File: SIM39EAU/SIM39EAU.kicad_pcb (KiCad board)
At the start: 2 copper layers, 30.5 x 25.4 mm, 17 parts, among them IC1 SIM39EA, J1 Conn_01x08, U2 AP7365-W-7

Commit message: LED Update
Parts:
- removed R7: 68K, Resistor_SMD:R_0603_1608Metric
- removed R8: 22K, Resistor_SMD:R_0603_1608Metric
- removed U2: AP7365-W-7, Package_TO_SOT_SMD:SOT-23-5
- added 3.3V: LED, LED_SMD:LED_0603_1608Metric, F.Cu at (53.1, 33.0)
- added LED: SolderJumper_2_Bridged, Jumper:SolderJumper-2_P1.3mm_Bridged_RoundedPad1.0x1.5mm, B.Cu at (56.3, 38.9)
- added R1: 680E, Resistor_SMD:R_0603_1608Metric, F.Cu at (53.1, 36.3)
- added U1: AP2127K-3.3, Package_TO_SOT_SMD:SOT-23-5, F.Cu at (55.8, 35.3)
- C4: value 1uF -> 4.7uF
- moved G*** 0.18 mm to (56.0, 27.3)
- renumbered CR1220 to BT1
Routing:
- net Net-(JP1-Pad2): track 0.00 -> 3.99 mm, vias 0 -> 1
- net Net-(R7-Pad2): track 3.84 -> 0.00 mm
- net Net-(D3-Pad2): track 0.00 -> 1.75 mm
- net 3V3: track 5.04 -> 3.92 mm, vias 3 -> 2

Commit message: Schematic PDF and 3D Renders added
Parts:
- renumbered BT1 to CR1220
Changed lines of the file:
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@@
   )
   (setup
-    (last_trace_width 0.4)
+    (last_trace_width 0.127)
     (user_trace_width 0.127)
     (user_trace_width 0.15)
@@
     (tags "Keystone type 3000 coin cell retainer")
     (attr smd)
-    (fp_text reference BT1 (at 0 4.445 270 unlocked) (layer B.SilkS)
+    (fp_text reference CR1220 (at 0 4.445 270 unlocked) (layer B.SilkS)
       (effects (font (size 1 1) (thickness 0.15)) (justify mirror))
     )

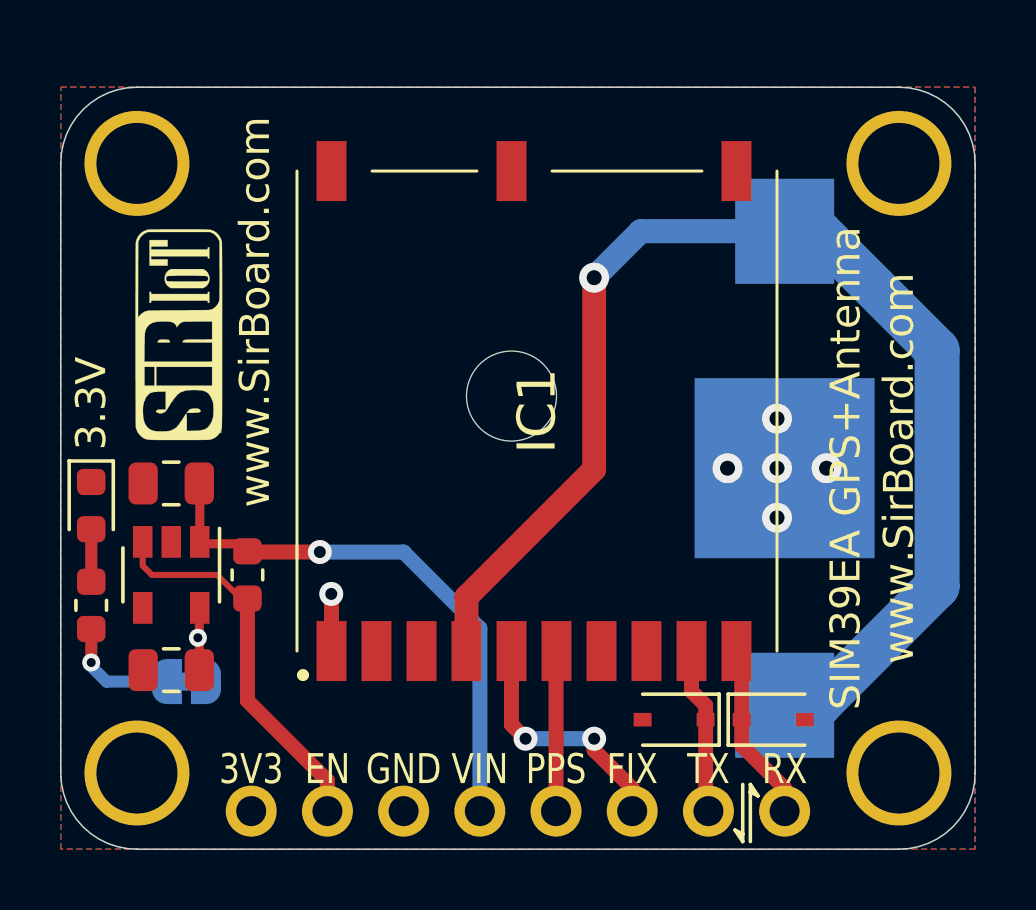
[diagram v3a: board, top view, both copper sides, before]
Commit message: Board Sizes Updated
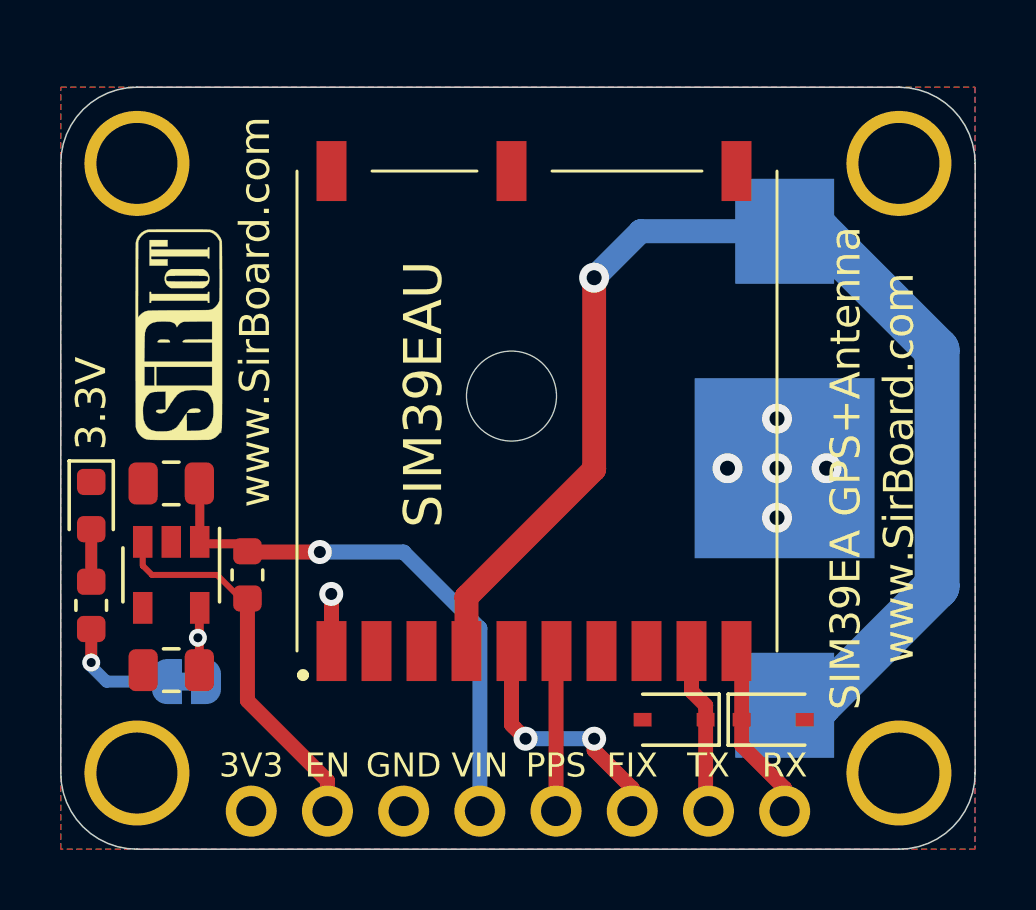
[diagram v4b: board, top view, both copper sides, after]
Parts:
- renumbered IC1 to SIM39EAU
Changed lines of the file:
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@@
   (general
     (thickness 1.6)
-    (drawings 34)
+    (drawings 26)
     (tracks 67)
     (zones 0)
@@
     (38 B.Mask user hide)
     (39 F.Mask user hide)
-    (40 Dwgs.User user hide)
+    (40 Dwgs.User user)
     (41 Cmts.User user hide)
     (42 Eco1.User user hide)
@@
     (descr SIM39EA-2)
     (tags "Integrated Circuit")
-    (fp_text reference IC1 (at 0 0 90) (layer F.SilkS)
+    (fp_text reference SIM39EAU (at 0.5588 -3.7846 90) (layer F.SilkS)
       (effects (font (size 1.27 1.27) (thickness 0.254)))
     )
@@
     )
   )
+  (gr_line (start 54.61 44.45) (end 80.01 44.45) (layer Edge.Cuts) (width 0.05))
   (gr_text www.SirBoard.com (at 58.547 26.543 90) (layer F.SilkS)
     (effects (font (size 1 1) (thickness 0.15)))
@@
     (effects (font (size 1 1) (thickness 0.15)))
   )
-  (gr_line (start 75.057 42.545) (end 75.184 42.545) (layer F.SilkS) (width 0.12))
-  (gr_line (start 75.311 42.672) (end 75.057 42.545) (layer F.SilkS) (width 0.12))
-  (gr_line (start 75.057 42.291) (end 75.311 42.672) (layer F.SilkS) (width 0.12))
-  (gr_line (start 75.057 44.196) (end 75.057 42.291) (layer F.SilkS) (width 0.12))
-  (gr_line (start 74.803 43.942) (end 74.676 43.942) (layer F.SilkS) (width 0.12))
-  (gr_line (start 74.549 43.815) (end 74.803 43.942) (layer F.SilkS) (width 0.12))
-  (gr_line (start 74.803 44.196) (end 74.549 43.815) (layer F.SilkS) (width 0.12))
-  (gr_line (start 74.803 42.291) (end 74.803 44.196) (layer F.SilkS) (width 0.12))
-  (gr_text FIX (at 71.12 41.783) (layer F.SilkS)
-    (effects (font (size 1 0.8) (thickness 0.15)))
+  (gr_text FIX (at 71.12 41.656) (layer F.SilkS)
+    (effects (font (size 0.8 0.8) (thickness 0.12)))
   )
   (dimension 20.32 (width 0.15) (layer Dwgs.User)
@@
     (arrow2b (pts (xy 58.42 46.99) (xy 59.546504 46.403579)))
   )
-  (gr_text VIN (at 66.04 41.783) (layer F.SilkS)
-    (effects (font (size 1 0.8) (thickness 0.15)))
-  )
-  (gr_text GND (at 63.5 41.783) (layer F.SilkS)
-    (effects (font (size 1 0.8) (thickness 0.15)))
-  )
-  (gr_text EN (at 60.96 41.783) (layer F.SilkS)
-    (effects (font (size 1 0.8) (thickness 0.15)))
+  (gr_text VIN (at 66.04 41.656) (layer F.SilkS)
+    (effects (font (size 0.8 0.8) (thickness 0.12)))
+  )
+  (gr_text GND (at 63.5 41.656) (layer F.SilkS)
+    (effects (font (size 0.8 0.8) (thickness 0.12)))
+  )
+  (gr_text EN (at 60.96 41.656) (layer F.SilkS)
+    (effects (font (size 0.8 0.8) (thickness 0.12)))
   )
   (dimension 30.48 (width 0.12) (layer Dwgs.User)
@@
     (arrow2b (pts (xy 86.36 44.45) (xy 85.773579 43.323496)))
   )
-  (gr_text RX (at 76.2 41.783) (layer F.SilkS)
-    (effects (font (size 1 0.8) (thickness 0.15)))
-  )
-  (gr_text PPS (at 68.58 41.783) (layer F.SilkS)
-    (effects (font (size 1 0.8) (thickness 0.15)))
-  )
-  (gr_text TX (at 73.66 41.783) (layer F.SilkS)
-    (effects (font (size 1 0.8) (thickness 0.15)))
-  )
-  (gr_text 3V3 (at 58.42 41.783) (layer F.SilkS)
-    (effects (font (size 1 0.8) (thickness 0.15)))
+  (gr_text RX (at 76.2 41.656) (layer F.SilkS)
+    (effects (font (size 0.8 0.8) (thickness 0.12)))
+  )
+  (gr_text PPS (at 68.58 41.656) (layer F.SilkS)
+    (effects (font (size 0.8 0.8) (thickness 0.12)))
+  )
+  (gr_text TX (at 73.66 41.656) (layer F.SilkS)
+    (effects (font (size 0.8 0.8) (thickness 0.12)))
+  )
+  (gr_text 3V3 (at 58.42 41.656) (layer F.SilkS)
+    (effects (font (size 0.8 0.8) (thickness 0.12)))
   )
   (gr_line (start 52.07 21.59) (end 52.07 41.91) (layer Edge.Cuts) (width 0.05))
@@
   (gr_line (start 82.55 41.91) (end 82.55 21.59) (layer Edge.Cuts) (width 0.05))
   (gr_arc (start 80.01 41.91) (end 80.01 44.45) (angle -90) (layer Edge.Cuts) (width 0.05))
-  (gr_line (start 54.61 44.45) (end 80.01 44.45) (layer Edge.Cuts) (width 0.05))
   (gr_arc (start 54.61 41.91) (end 52.07 41.91) (angle -90) (layer Edge.Cuts) (width 0.05))
   (via (at 75.946 31.75) (size 1) (drill 0.5) (layers F.Cu B.Cu) (net 1))
@@
   (segment (start 53.086 38.354) (end 53.594 38.862) (width 0.4) (layer B.Cu) (net 13))
   (zone (net 1) (net_name GND) (layer F.Cu) (hatch none 0.508)
-    (connect_pads (clearance 0.15))
+    (connect_pads (clearance 0.2))
     (min_thickness 0.15)
     (fill yes (arc_segments 32) (thermal_gap 0.2) (thermal_bridge_width 0.25))

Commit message: Soldermask width adjusted
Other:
- rule solder_mask_min_width: 0.1 -> 0.05
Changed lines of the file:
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@@
     (pad_drill 1)
     (pad_to_mask_clearance 0)
-    (solder_mask_min_width 0.1)
+    (solder_mask_min_width 0.05)
     (aux_axis_origin 0 0)
     (visible_elements 7FFFFFFF)

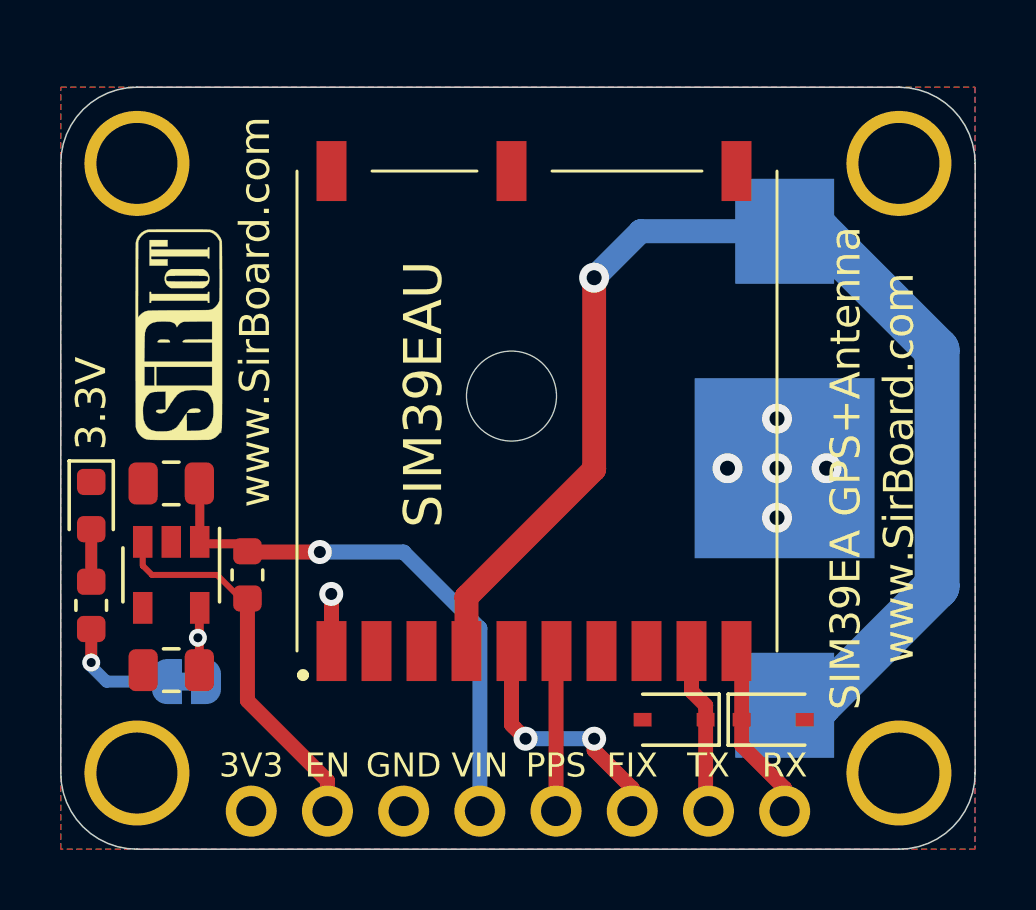
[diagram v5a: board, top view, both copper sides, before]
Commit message: SIM39EA Revision 2
Battery connector changed and silkscreens rearranged
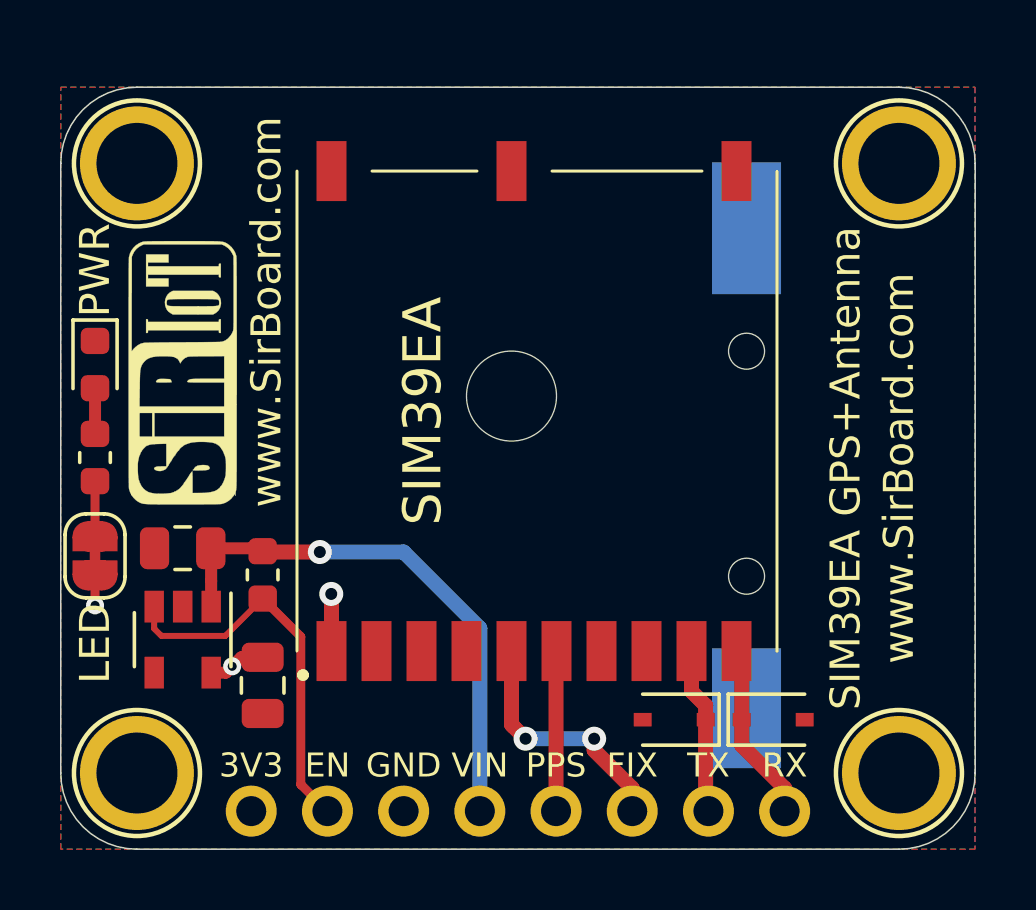
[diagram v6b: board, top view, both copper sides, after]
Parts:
- added G***: LOGO, logo:logo94x134, B.Cu at (62.7, 29.5)
- added REF**: OSHW-Logo2_7.3x6mm_SilkScreen, Symbol:OSHW-Logo2_7.3x6mm_SilkScreen, B.Cu at (56.1, 29.6)
- C3: value 1uF -> 10uF
- C4: value 4.7uF -> 10uF
- CR1220: footprint Battery:BatteryHolder_Keystone_3000_1x12mm -> SirBoardLibrary:S8411-45R_1
- G***: footprint logo:SirIoT98x40 -> logo:SirBoard140x44
- G***: footprint logo:SirIoT70x29 -> logo:SirIoT88x36
- H1, H2, H3, H4: footprint MountingHole:MountingHole_2.7mm_M2.5_ISO14580_Pad -> SirBoardLibrary:MountingHole_M2.5_SirBoard
- LED: footprint Jumper:SolderJumper-2_P1.3mm_Bridged_RoundedPad1.0x1.5mm -> SirBoardLibrary:SolderJumper-2_P1.3mm_Bridged_RoundedPad1.0x1.5mm; moved to F.Cu
- moved G*** 6.04 mm to (59.8, 37.3), turned to 180 degrees
- moved LED 5.18 mm to (53.2, 34.7), turned to 90 degrees
- moved R1 4.93 mm to (53.2, 31.4)
- moved PWR 4.70 mm to (53.2, 28.3)
- moved C4 3.09 mm to (58.8, 39.0), turned to 270 degrees
- moved U1 2.19 mm to (56.1, 37.5)
- moved C3 2.19 mm to (56.1, 34.4)
- moved G*** 1.28 mm to (56.1, 28.6)
- moved CR1220 1.27 mm to (74.9, 31.8), turned to 0 degrees
- moved R3 0.51 mm to (58.8, 35.3)
- renumbered 3.3V to PWR, SIM39EAU to SIM39EA
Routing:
- net Net-(BT1-Pad1): track 42.5 -> 0.00 mm, vias 1 -> 0
- net Net-(JP1-Pad2): track 3.99 -> 1.84 mm, vias 1 -> 0
- net 3V3: track 3.92 -> 5.03 mm, vias 2 -> 3
- net GND: vias 5 -> 0

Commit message: SIM39EA Revision 2
Battery Connected
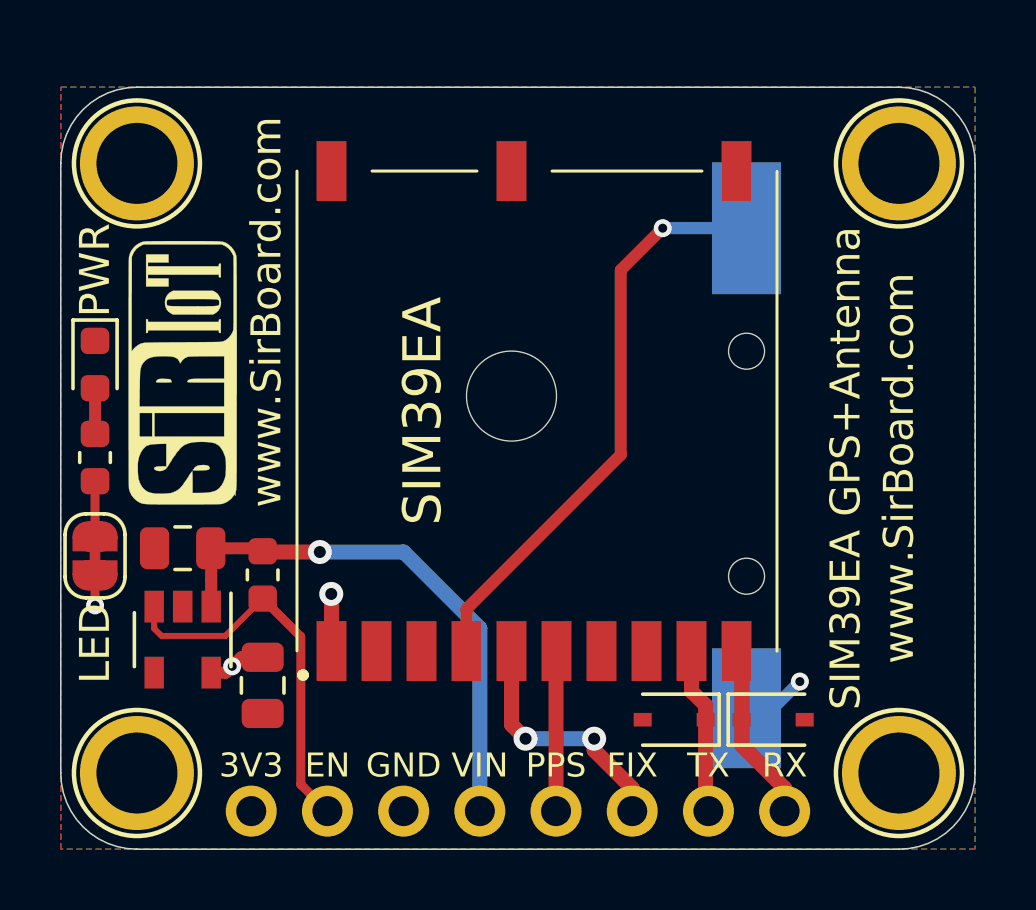
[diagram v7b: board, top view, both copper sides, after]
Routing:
- net Net-(BT1-Pad1): track 0.00 -> 19.6 mm, vias 0 -> 1
- net GND: track 0.00 -> 2.15 mm, vias 0 -> 1
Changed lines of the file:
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@@
   (general
     (thickness 1.6)
-    (drawings 27)
-    (tracks 55)
+    (drawings 26)
+    (tracks 65)
     (zones 0)
     (modules 20)
@@
     (effects (font (size 1 1) (thickness 0.15)) (justify mirror))
   )
-  (dimension 12.7 (width 0.15) (layer Dwgs.User)
-    (gr_text "12.700 mm" (at 96.55 25.4 270) (layer Dwgs.User)
-      (effects (font (size 1 1) (thickness 0.15)))
-    )
-    (feature1 (pts (xy 52.07 31.75) (xy 95.836421 31.75)))
-    (feature2 (pts (xy 52.07 19.05) (xy 95.836421 19.05)))
-    (crossbar (pts (xy 95.25 19.05) (xy 95.25 31.75)))
-    (arrow1a (pts (xy 95.25 31.75) (xy 94.663579 30.623496)))
-    (arrow1b (pts (xy 95.25 31.75) (xy 95.836421 30.623496)))
-    (arrow2a (pts (xy 95.25 19.05) (xy 94.663579 20.176504)))
-    (arrow2b (pts (xy 95.25 19.05) (xy 95.836421 20.176504)))
-  )
   (gr_line (start 54.61 44.45) (end 80.01 44.45) (layer Edge.Cuts) (width 0.05))
   (gr_text www.SirBoard.com (at 58.928 26.543 90) (layer F.SilkS)
@@
   (gr_arc (start 80.01 41.91) (end 80.01 44.45) (angle -90) (layer Edge.Cuts) (width 0.05))
   (gr_arc (start 54.61 41.91) (end 52.07 41.91) (angle -90) (layer Edge.Cuts) (width 0.05))
+  (via (at 76.708 38.862) (size 0.6) (drill 0.3) (layers F.Cu B.Cu) (net 1))
+  (segment (start 74.93 39.75) (end 75.82 39.75) (width 0.4) (layer B.Cu) (net 1))
+  (segment (start 75.82 39.75) (end 76.708 38.862) (width 0.4) (layer B.Cu) (net 1))
   (segment (start 57.0715 38.641) (end 57.084 38.6285) (width 0.3) (layer F.Cu) (net 2))
   (via (at 61.087 35.941) (size 0.8) (drill 0.4) (layers F.Cu B.Cu) (net 2))
@@
   (segment (start 57.5565 37.338) (end 58.801 36.0935) (width 0.2) (layer F.Cu) (net 7))
   (segment (start 55.427 37.338) (end 57.5565 37.338) (width 0.2) (layer F.Cu) (net 7))
+  (segment (start 65.595 36.445) (end 70.739 31.301) (width 0.4) (layer F.Cu) (net 8))
+  (segment (start 65.595 37.845) (end 65.595 36.445) (width 0.4) (layer F.Cu) (net 8))
+  (via (at 72.136 23.749) (size 0.6) (drill 0.3) (layers F.Cu B.Cu) (net 8))
+  (segment (start 70.739 31.301) (end 70.739 25.146) (width 0.4) (layer F.Cu) (net 8))
+  (segment (start 70.739 25.146) (end 72.136 23.749) (width 0.4) (layer F.Cu) (net 8))
+  (segment (start 74.929 23.749) (end 74.93 23.75) (width 0.4) (layer B.Cu) (net 8))
+  (segment (start 72.136 23.749) (end 74.929 23.749) (width 0.4) (layer B.Cu) (net 8))
   (segment (start 76.2 42.418) (end 76.2 43.18) (width 0.5) (layer F.Cu) (net 9))
   (segment (start 74.769 40.987) (end 76.2 42.418) (width 0.5) (layer F.Cu) (net 9))
